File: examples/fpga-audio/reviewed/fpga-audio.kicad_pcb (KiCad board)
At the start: 2 copper layers, 94 x 84 mm, 29 parts, among them J1 3V3 IN, J2 AUDIO OUT, J3 SPI PROG, U1 iCE40UP5K, U2 PCM5102A, U3 AP2112K-1.2, U4 W25Q32JV, X1 12MHz

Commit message: Route the sheets, and anchor the ground vias where the loop is
The user's verdict on the last round stood: none of the five schematics
read as a human drawing, and the artwork still had its physics wrong.
This round answers both.

The schematic side replaces the stub-and-label sheet with a router.
Every signal net becomes a tree of straight, L-, Z- and detour-shaped
runs on the 1.27 mm grid: legs leave a pin along its own stub, escape
distances stagger so a bus does not fight over one column, every pin
reserves a runway another wire may cross but not ride along, and the
sheet frame, title block and notes are obstacles like any symbol.
Fragments merge Kruskal-style so a rail whose regulator is boxed in
still gets its capacitors chained; each surviving fragment keeps one
label, because the label is what names the net. Collinear same-net
segments are unioned and then split at every tee - KiCad 9's
connectivity requires files drawn the way the editor draws them, with
a junction dot and a wire break wherever a branch tees in, and a wire
that runs through a junction connects on one side of it only. That
last fact cost an evening and is now a comment.

Trying to draw the wires found what no rule had: the buck's LED was
upside down with its ground pointing up into the resistor above it,
both breakout headers faced away from everything they connect to
(fixed with mirrored symbols, which Part now supports), the FPGA
sheet's notes printed over the 1.2 V regulator, and its programming
header sat inside the title block. Wired: buck, motor and op-amp
completely; the Pico carrier 31 of 33 nets; the FPGA board 16 of 19 -
what stays labelled is what a human would label too.

The artwork side anchors every FPGA decoupling capacitor's ground via
against its own pad, on the far side from the supply pad, with the
1.2 mm stub as the whole loop - retiring all seven
layout.decoupling_via findings and that waiver with them. A back_cost
experiment (0.4 to 0.6) to shrink the return-path cuts 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
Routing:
- net /CRESET: track 104.7 -> 123.4 mm, vias 3 -> 6
- net GND: track 168.7 -> 153.3 mm
- net /I2S_LRCK: track 45.0 -> 30.4 mm
- net /SPI_SS: track 93.9 -> 106.7 mm, vias 4 -> 2
- net /SPI_SCK: track 70.0 -> 78.2 mm, vias 2 -> 0
- net /SPI_SO: track 82.9 -> 78.3 mm, vias 2 -> 4
- net /VCCPLL: track 44.8 -> 42.4 mm
- net /LDOO: track 20.1 -> 22.3 mm
- net /SPI_SI: track 70.5 -> 68.6 mm, vias 2 -> 4
- net /I2S_DIN: track 28.7 -> 27.1 mm, vias 2 -> 0
- net /+1V2: track 104.2 -> 105.2 mm
- net /I2S_SCK: track 30.0 -> 29.4 mm
- net +3V3: track 561.6 -> 561.4 mm, vias 4 -> 8

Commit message: Regenerate the five with stitched pours, silk that speaks, and wires that never double back
All ten variants rebuilt by the fixed generator: reviewed boards carry
ground on both faces with the stitching ring (buck 35 vias, fpga 116),
thru_hole_only front pours, the board id and connector pin names in
silk, and the buck's explicit ground return; the sheets hook power up
through upright symbols and source-anchored flags with no overlapping
wires and no junction-less tees left. Every reviewed variant passes its
own gate with zero errors; every as-generated variant still fails, now
also for the rules this round added.

Co-Authored-By: Claude Fable 5 <noreply@anthropic.com>
Claude-Session: https://claude.ai/code/session_01DUj7Ltu92tWg159mCSacwY
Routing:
- net GND: vias 37 -> 67
- added copper zone on F.Cu, net GND
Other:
- board text added: "+3V3"
- board text added: "CRESET"
- board text added: "GND"
- board text added: "OUTL"
- board text added: "OUTR"
- board text added: "SPI_SCK"
- board text added: "SPI_SI"
- board text added: "SPI_SO"
- board text added: "SPI_SS"
- board text added: "fpga-audio rev A"
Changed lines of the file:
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@@
 	(via (at 187.25 97.5) (size 0.8) (drill 0.4) (layers "F.Cu" "B.Cu") (net 1))
 	(via (at 178.0 130.0) (size 0.8) (drill 0.4) (layers "F.Cu" "B.Cu") (net 1))
+	(via (at 104.5 64.5) (size 0.8) (drill 0.4) (layers "F.Cu" "B.Cu") (net 1))
+	(via (at 104.5 139.5) (size 0.8) (drill 0.4) (layers "F.Cu" "B.Cu") (net 1))
+	(via (at 114.5 64.5) (size 0.8) (drill 0.4) (layers "F.Cu" "B.Cu") (net 1))
+	(via (at 114.5 139.5) (size 0.8) (drill 0.4) (layers "F.Cu" "B.Cu") (net 1))
+	(via (at 124.5 64.5) (size 0.8) (drill 0.4) (layers "F.Cu" "B.Cu") (net 1))
+	(via (at 124.5 139.5) (size 0.8) (drill 0.4) (layers "F.Cu" "B.Cu") (net 1))
+	(via (at 134.5 64.5) (size 0.8) (drill 0.4) (layers "F.Cu" "B.Cu") (net 1))
+	(via (at 134.5 139.5) (size 0.8) (drill 0.4) (layers "F.Cu" "B.Cu") (net 1))
+	(via (at 144.5 64.5) (size 0.8) (drill 0.4) (layers "F.Cu" "B.Cu") (net 1))
+	(via (at 144.5 139.5) (size 0.8) (drill 0.4) (layers "F.Cu" "B.Cu") (net 1))
+	(via (at 154.5 64.5) (size 0.8) (drill 0.4) (layers "F.Cu" "B.Cu") (net 1))
+	(via (at 154.5 139.5) (size 0.8) (drill 0.4) (layers "F.Cu" "B.Cu") (net 1))
+	(via (at 164.5 64.5) (size 0.8) (drill 0.4) (layers "F.Cu" "B.Cu") (net 1))
+	(via (at 164.5 139.5) (size 0.8) (drill 0.4) (layers "F.Cu" "B.Cu") (net 1))
+	(via (at 174.5 64.5) (size 0.8) (drill 0.4) (layers "F.Cu" "B.Cu") (net 1))
+	(via (at 184.5 64.5) (size 0.8) (drill 0.4) (layers "F.Cu" "B.Cu") (net 1))
+	(via (at 184.5 139.5) (size 0.8) (drill 0.4) (layers "F.Cu" "B.Cu") (net 1))
+	(via (at 104.5 74.5) (size 0.8) (drill 0.4) (layers "F.Cu" "B.Cu") (net 1))
+	(via (at 189.5 74.5) (size 0.8) (drill 0.4) (layers "F.Cu" "B.Cu") (net 1))
+	(via (at 104.5 84.5) (size 0.8) (drill 0.4) (layers "F.Cu" "B.Cu") (net 1))
+	(via (at 189.5 84.5) (size 0.8) (drill 0.4) (layers "F.Cu" "B.Cu") (net 1))
+	(via (at 104.5 94.5) (size 0.8) (drill 0.4) (layers "F.Cu" "B.Cu") (net 1))
+	(via (at 189.5 94.5) (size 0.8) (drill 0.4) (layers "F.Cu" "B.Cu") (net 1))
+	(via (at 104.5 104.5) (size 0.8) (drill 0.4) (layers "F.Cu" "B.Cu") (net 1))
+	(via (at 104.5 114.5) (size 0.8) (drill 0.4) (layers "F.Cu" "B.Cu") (net 1))
+	(via (at 189.5 114.5) (size 0.8) (drill 0.4) (layers "F.Cu" "B.Cu") (net 1))
+	(via (at 104.5 124.5) (size 0.8) (drill 0.4) (layers "F.Cu" "B.Cu") (net 1))
+	(via (at 189.5 124.5) (size 0.8) (drill 0.4) (layers "F.Cu" "B.Cu") (net 1))
+	(via (at 104.5 134.5) (size 0.8) (drill 0.4) (layers "F.Cu" "B.Cu") (net 1))
+	(via (at 189.5 134.5) (size 0.8) (drill 0.4) (layers "F.Cu" "B.Cu") (net 1))
 	(zone
 		(net 1)
@@
 		(polygon (pts (xy 103.0 63.0) (xy 191.0 63.0) (xy 191.0 141.0) (xy 103.0 141.0)))
 	)
+	(zone
+		(net 1)
+		(net_name "GND")
+		(layer "F.Cu")
+		(hatch edge 0.5)
+		(connect_pads thru_hole_only
+			(clearance 0.4)
+		)
+		(min_thickness 0.175)
+		(filled_areas_thickness no)
+		(fill yes
+			(thermal_gap 0.5)
+			(thermal_bridge_width 0.5)
+		)
+		(polygon (pts (xy 103.0 63.0) (xy 191.0 63.0) (xy 191.0 141.0) (xy 103.0 141.0)))
+	)
+	(gr_text "fpga-audio rev A" (at 147.0 141.8 0) (layer "F.SilkS") (effects (font (size 1.0 1.0) (thickness 0.15))))
+	(gr_text "+3V3" (at 115.31 68.0 0) (layer "F.SilkS") (effects (font (size 0.8 0.8) (thickness 0.12))))
+	(gr_text "GND" (at 115.31 73.0 0) (layer "F.SilkS") (effects (font (size 0.8 0.8) (thickness 0.12))))
+	(gr_text "OUTR" (at 185.63 98.0 0) (layer "F.SilkS") (effects (font (size 0.8 0.8) (thickness 0.12))))
+	(gr_text "GND" (at 185.63 100.54 0) (layer "F.SilkS") (effects (font (size 0.8 0.8) (thickness 0.12))))
+	(gr_text "OUTL" (at 185.63 103.08 0) (layer "F.SilkS") (effects (font (size 0.8 0.8) (thickness 0.12))))
+	(gr_text "SPI_SS" (at 170.63 126.0 0) (layer "F.SilkS") (effects (font (size 0.8 0.8) (thickness 0.12))))
+	(gr_text "SPI_SCK" (at 170.63 128.54 0) (layer "F.SilkS") (effects (font (size 0.8 0.8) (thickness 0.12))))
+	(gr_text "SPI_SI" (at 170.63 131.08 0) (layer "F.SilkS") (effects (font (size 0.8 0.8) (thickness 0.12))))
+	(gr_text "SPI_SO" (at 170.63 133.62 0) (layer "F.SilkS") (effects (font (size 0.8 0.8) (thickness 0.12))))
+	(gr_text "CRESET" (at 170.63 136.16 0) (layer "F.SilkS") (effects (font (size 0.8 0.8) (thickness 0.12))))
+	(gr_text "GND" (at 170.63 138.7 0) (layer "F.SilkS") (effects (font (size 0.8 0.8) (thickness 0.12))))
 )

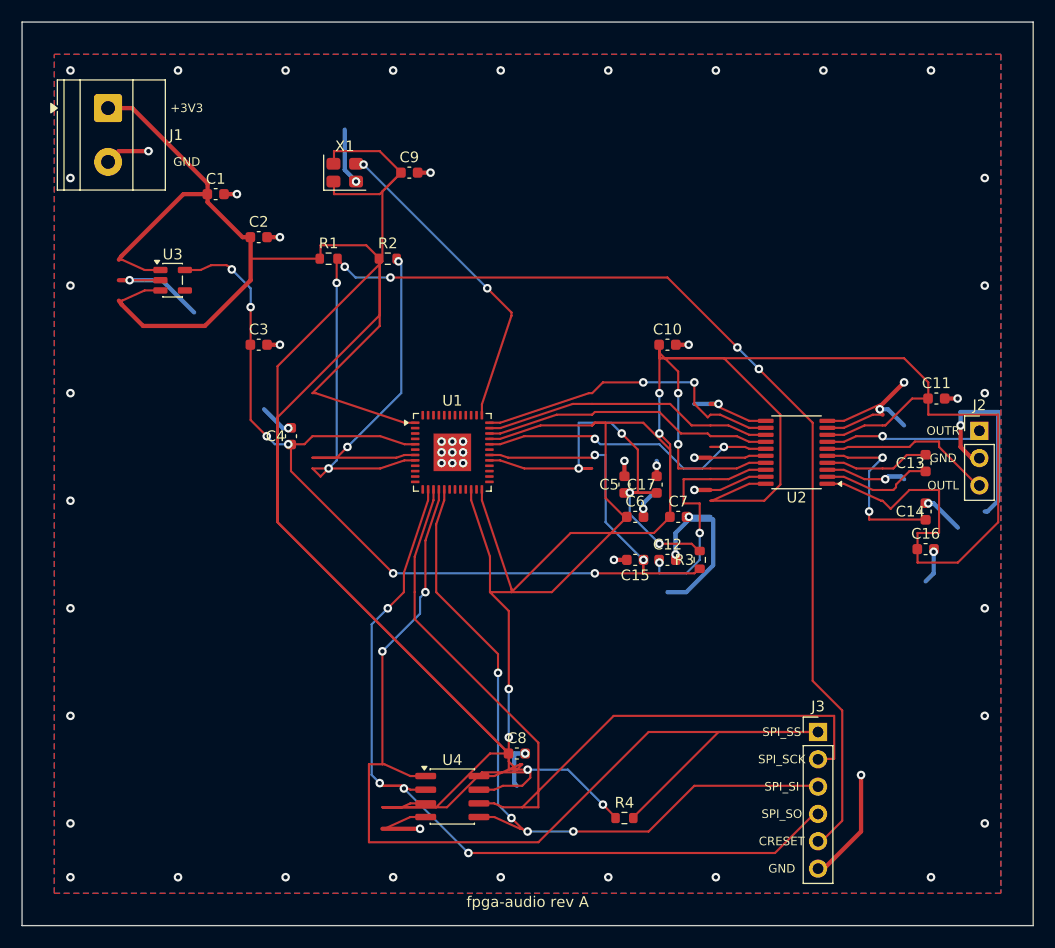
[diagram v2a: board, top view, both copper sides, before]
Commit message: Regenerate the five as round three drew them
All five reviewed projects pass their gates again: the buck all wire
with its feedback drawn home, the motor's logic named at the header,
the carrier reading as the pinout table it is - with its feed diode
finally pointing the right way - the filter compact with test points,
and the FPGA's capacitors sitting beside the units they feed. Thirty
renders redrawn, verdict tables at today's numbers.

Co-Authored-By: Claude Fable 5 <noreply@anthropic.com>
Claude-Session: https://claude.ai/code/session_01DUj7Ltu92tWg159mCSacwY
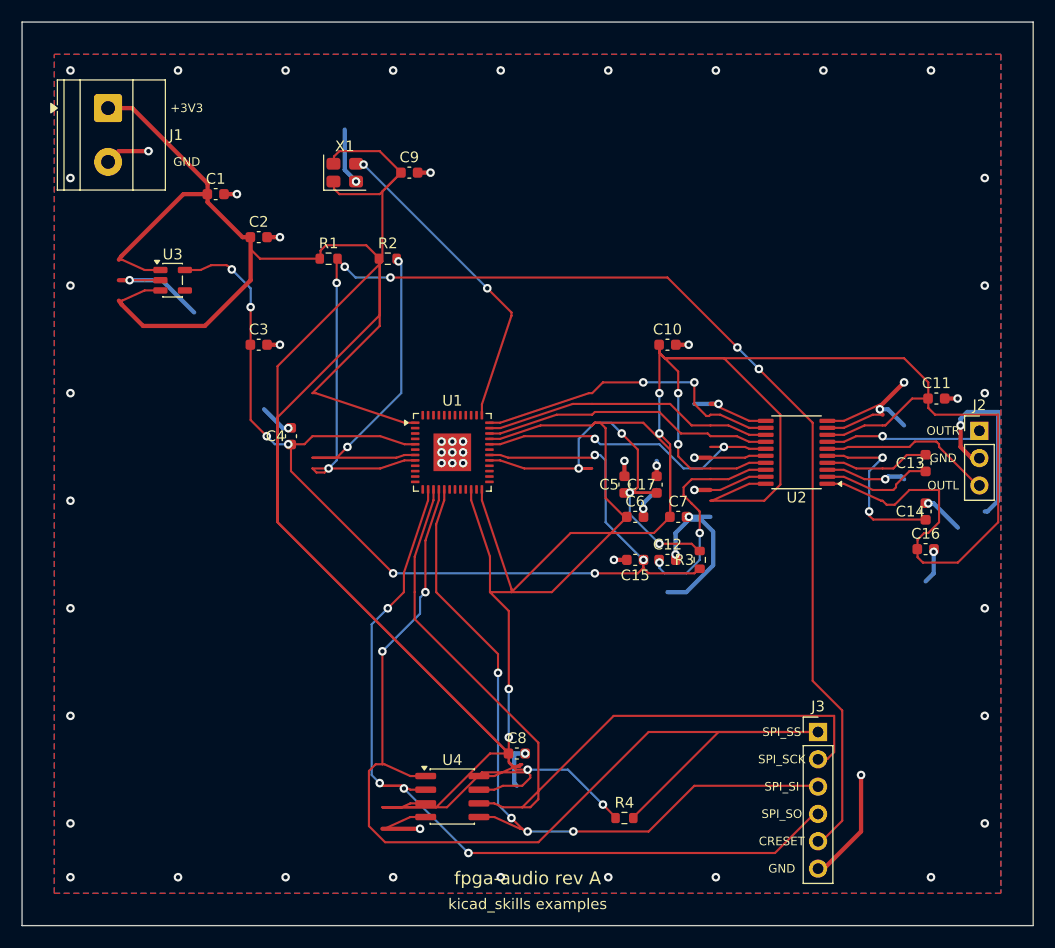
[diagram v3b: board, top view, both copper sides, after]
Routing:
- net +3V3: track 561.4 -> 555.8 mm
- net /LDOO: track 22.3 -> 20.7 mm
- net /SPI_SS: track 106.7 -> 105.4 mm
- net GND: track 153.3 -> 152.1 mm
- net /VCCPLL: track 42.4 -> 41.2 mm
- net /+1V2: track 105.2 -> 104.4 mm
- net /SPI_SCK: track 78.2 -> 77.4 mm
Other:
- board text added: "kicad_skills examples"

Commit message: Stitch the FPGA board's interior too
The same six millimetre ground mesh the other four boards now carry.
The schematic-side regeneration is still running and will follow.

Co-Authored-By: Claude Fable 5 <noreply@anthropic.com>
Claude-Session: https://claude.ai/code/session_01DUj7Ltu92tWg159mCSacwY
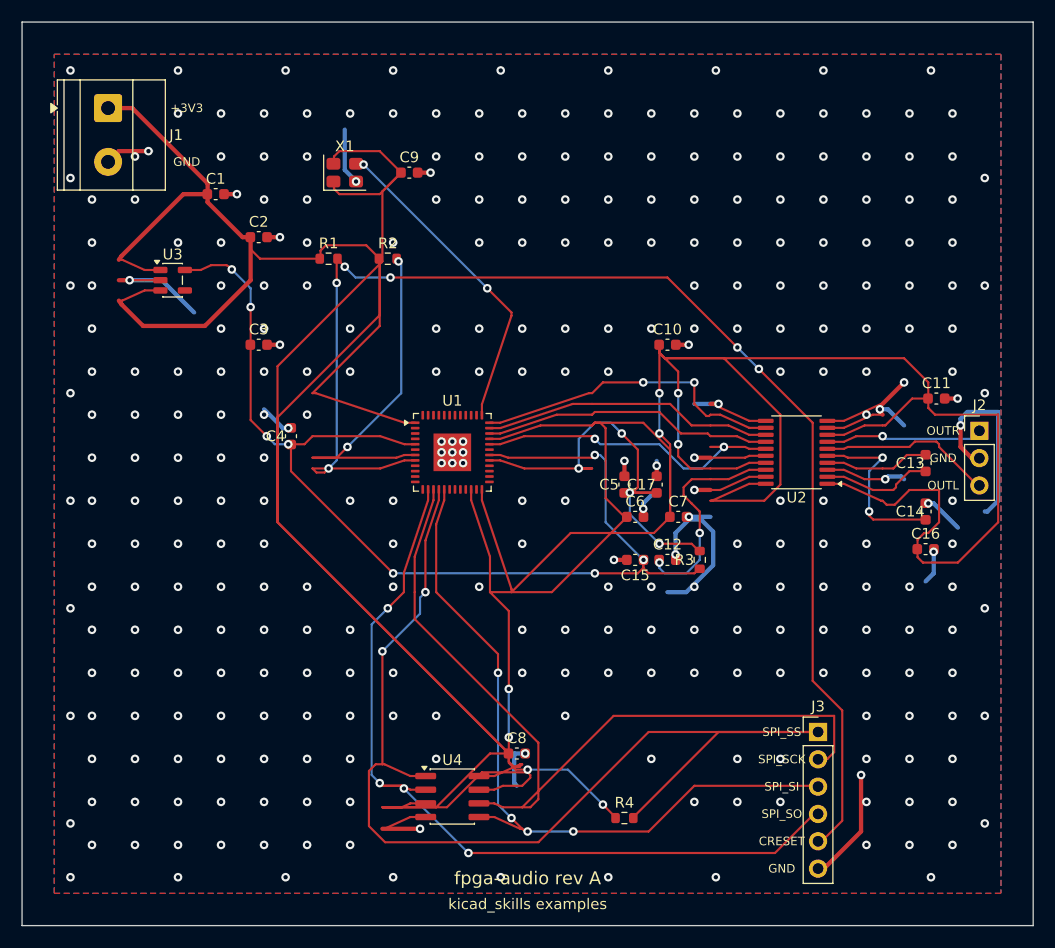
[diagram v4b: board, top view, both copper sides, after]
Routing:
- net GND: vias 67 -> 321

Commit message: Gather the FPGA sheet into blocks
Power, clock, config and codec each draw together with their own note
beside them, in place of parts spread over the whole of an A3 with
every net crossing the gap. The programming header comes off the title
block and the two long notes come back inside the frame.

Co-Authored-By: Claude Fable 5 <noreply@anthropic.com>
Claude-Session: https://claude.ai/code/session_01DUj7Ltu92tWg159mCSacwY
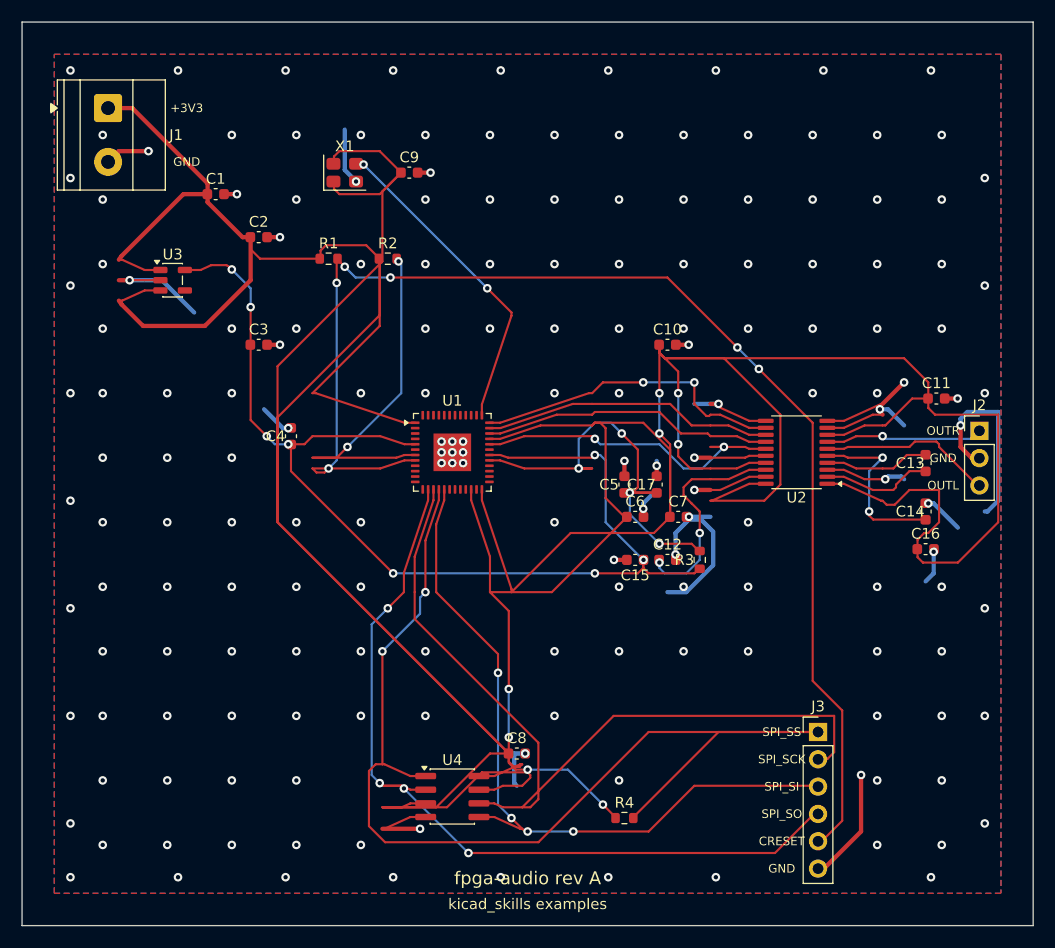
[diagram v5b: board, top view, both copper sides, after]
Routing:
- net GND: vias 321 -> 178

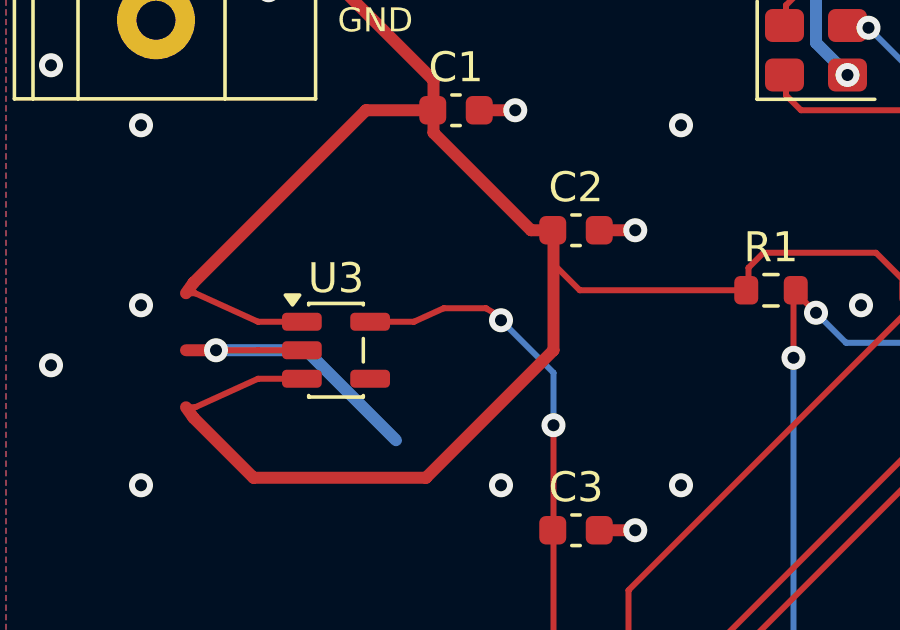
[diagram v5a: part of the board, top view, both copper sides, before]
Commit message: Regenerate the four the text and width work changed
Designators and values off the rails they were printed on, power-named
nets at the width their rule asks for, and the buck's feedback ending
on the capacitor pad it senses at.

Co-Authored-By: Claude Fable 5 <noreply@anthropic.com>
Claude-Session: https://claude.ai/code/session_01DUj7Ltu92tWg159mCSacwY
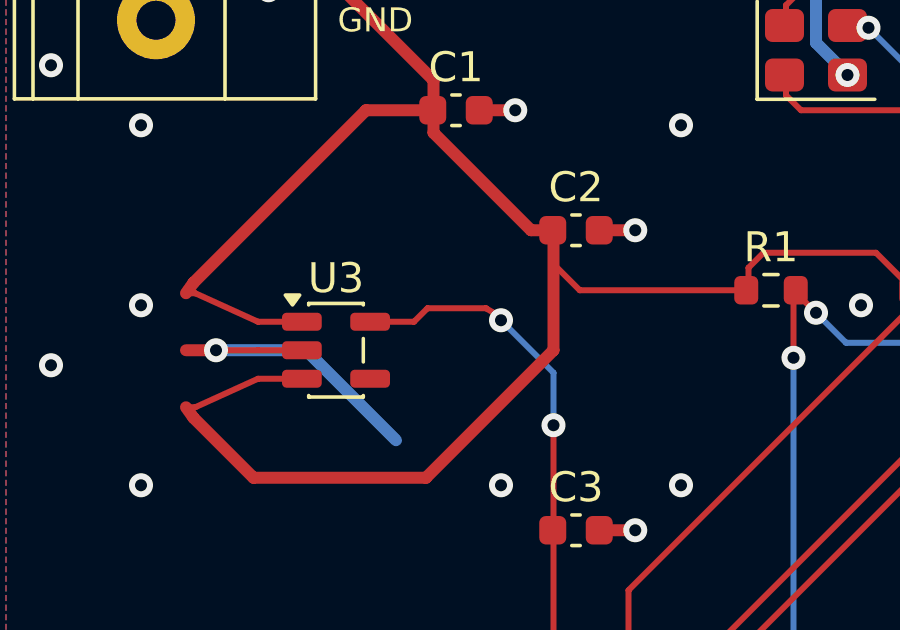
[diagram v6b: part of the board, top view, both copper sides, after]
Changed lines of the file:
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@@
 	(segment (start 109.31 85.9) (end 109.0 85.9) (width 0.2) (layer "F.Cu") (net 3))
 	(segment (start 115.1375 83.05) (end 116.6 83.05) (width 0.2) (layer "F.Cu") (net 2))
-	(segment (start 116.6 83.05) (end 117.59 82.6) (width 0.2) (layer "F.Cu") (net 2))
-	(segment (start 117.59 82.6) (end 119.0 82.6) (width 0.2) (layer "F.Cu") (net 2))
+	(segment (start 116.6 83.05) (end 117.05 82.6) (width 0.2) (layer "F.Cu") (net 2))
+	(segment (start 117.05 82.6) (end 119.0 82.6) (width 0.2) (layer "F.Cu") (net 2))
 	(segment (start 137.525 130.095) (end 136.1 130.095) (width 0.2) (layer "F.Cu") (net 19))
 	(segment (start 136.1 130.095) (end 133.691 129.0) (width 0.2) (layer "F.Cu") (net 19))
